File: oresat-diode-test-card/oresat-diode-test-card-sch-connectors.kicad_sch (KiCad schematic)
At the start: 13 parts, among them J1 J-SAMTEC-TFM-110-X1-XXX-D-RA, J2 U.FL, J3 U.FL, J4 U.FL, J6 J-SAMTEC-TFM-120-X1-XXX-D-RA

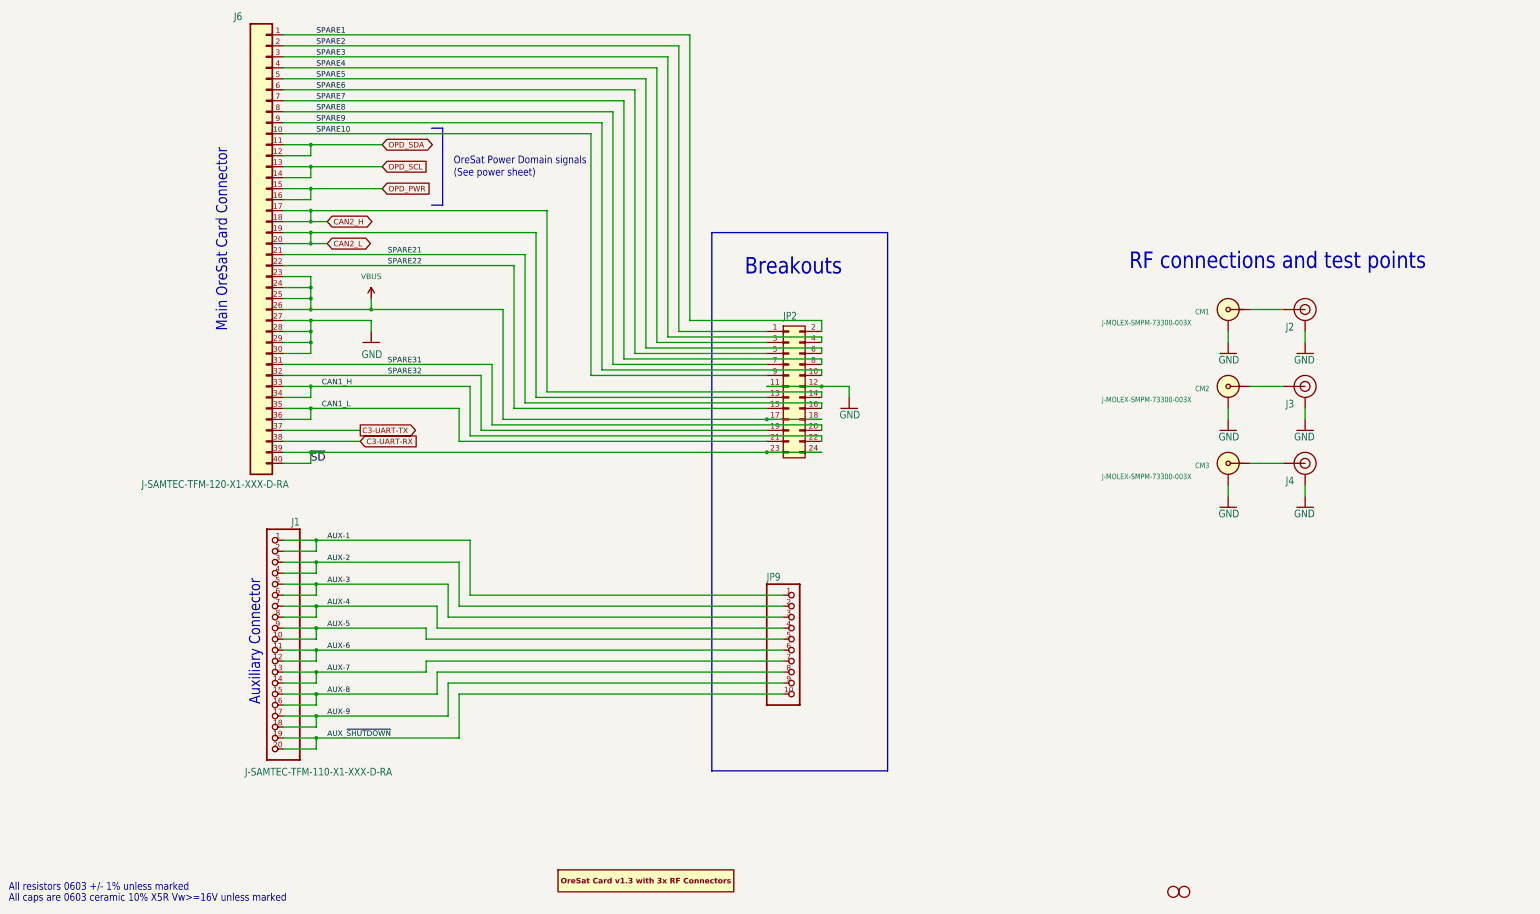
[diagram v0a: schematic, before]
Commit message: added photodiode and mux on schematic
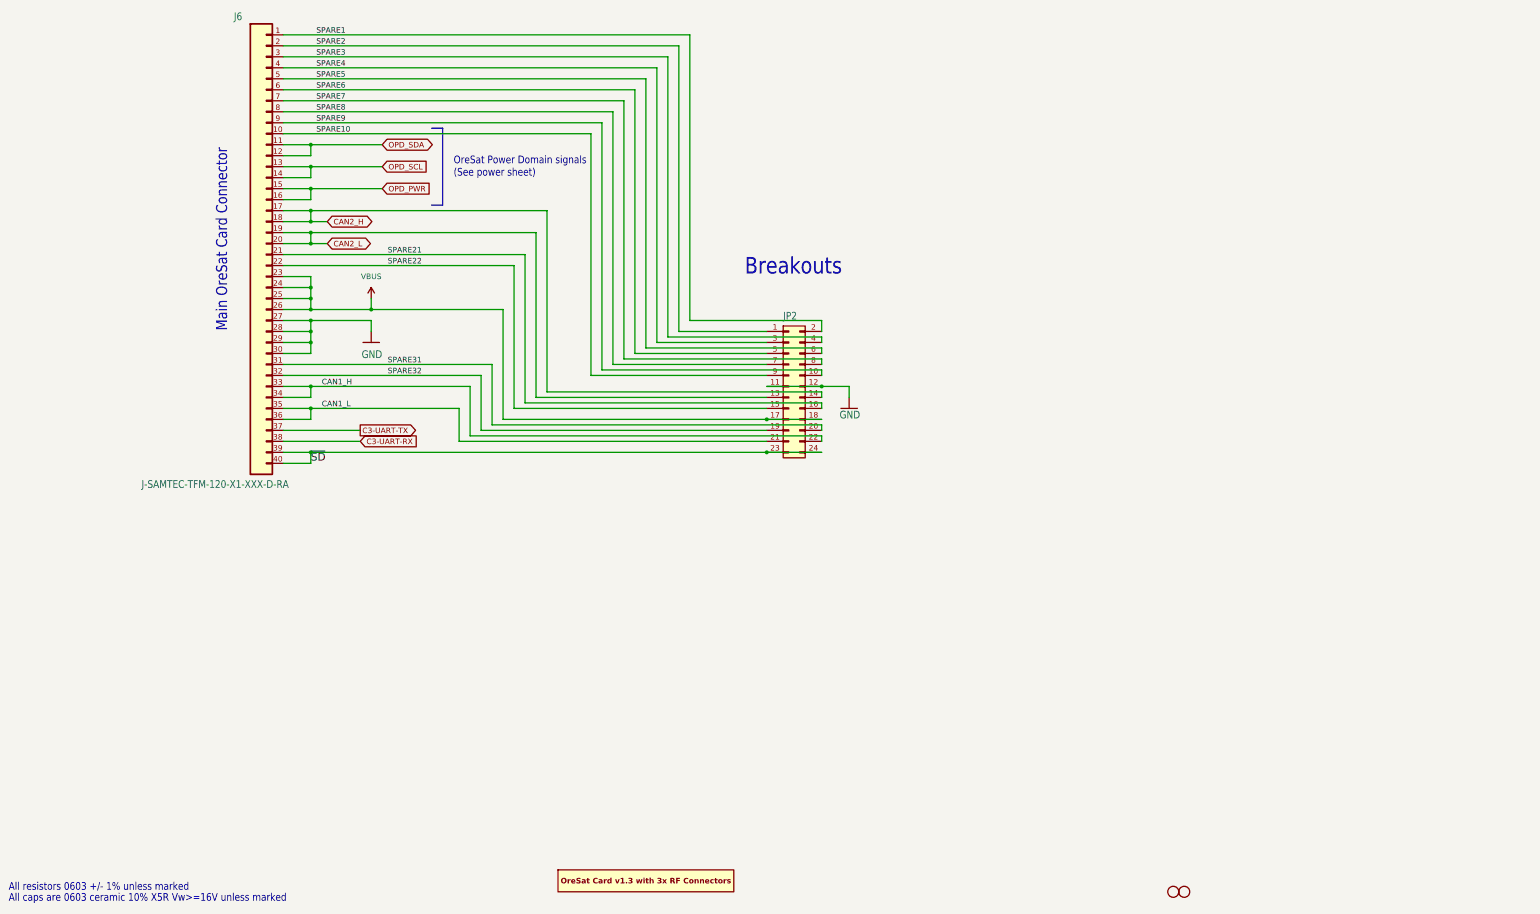
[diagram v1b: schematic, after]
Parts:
- removed CM1, CM2, CM3: J-MOLEX-SMPM-73300-003X, oresat-connectors:J-MOLEX-SMPM-073300-002X, symbol oresat-connectors:J-MOLEX-SMPM-73300-002X
- removed J1: J-SAMTEC-TFM-110-X1-XXX-D-RA, oresat-proto-card:J-SAMTEC-TFM-110-X1-XXX-D-RA, symbol oresat-proto-card-eagle-import:J-SAMTEC-TFM-110-X1-XXX-D-RA
- removed J2, J3, J4: U.FL, oresat-connectors:J-U.FL, symbol oresat-connectors:U.FL2PIN
- removed JP9: PINHD-1X10, oresat-proto-card:1X10, symbol oresat-proto-card-eagle-import:PINHD-1X10
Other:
- note removed: "Auxiliary Connector"
- note removed: "RF connections and test points"

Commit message: Quick design review on schematic; basically ready for layout.
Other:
- title: OreSat M0 Proto Card: Connectors -> OreSat Diode Test Card
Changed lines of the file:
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@@
 	(paper "USLedger")
 	(title_block
-		(title "OreSat M0 Proto Card: Connectors")
-		(date "2024-03-21")
-		(rev "5.0")
+		(title "OreSat Diode Test Card")
+		(date "2024-04-21")
+		(rev "v1.0")
 	)
 	(junction

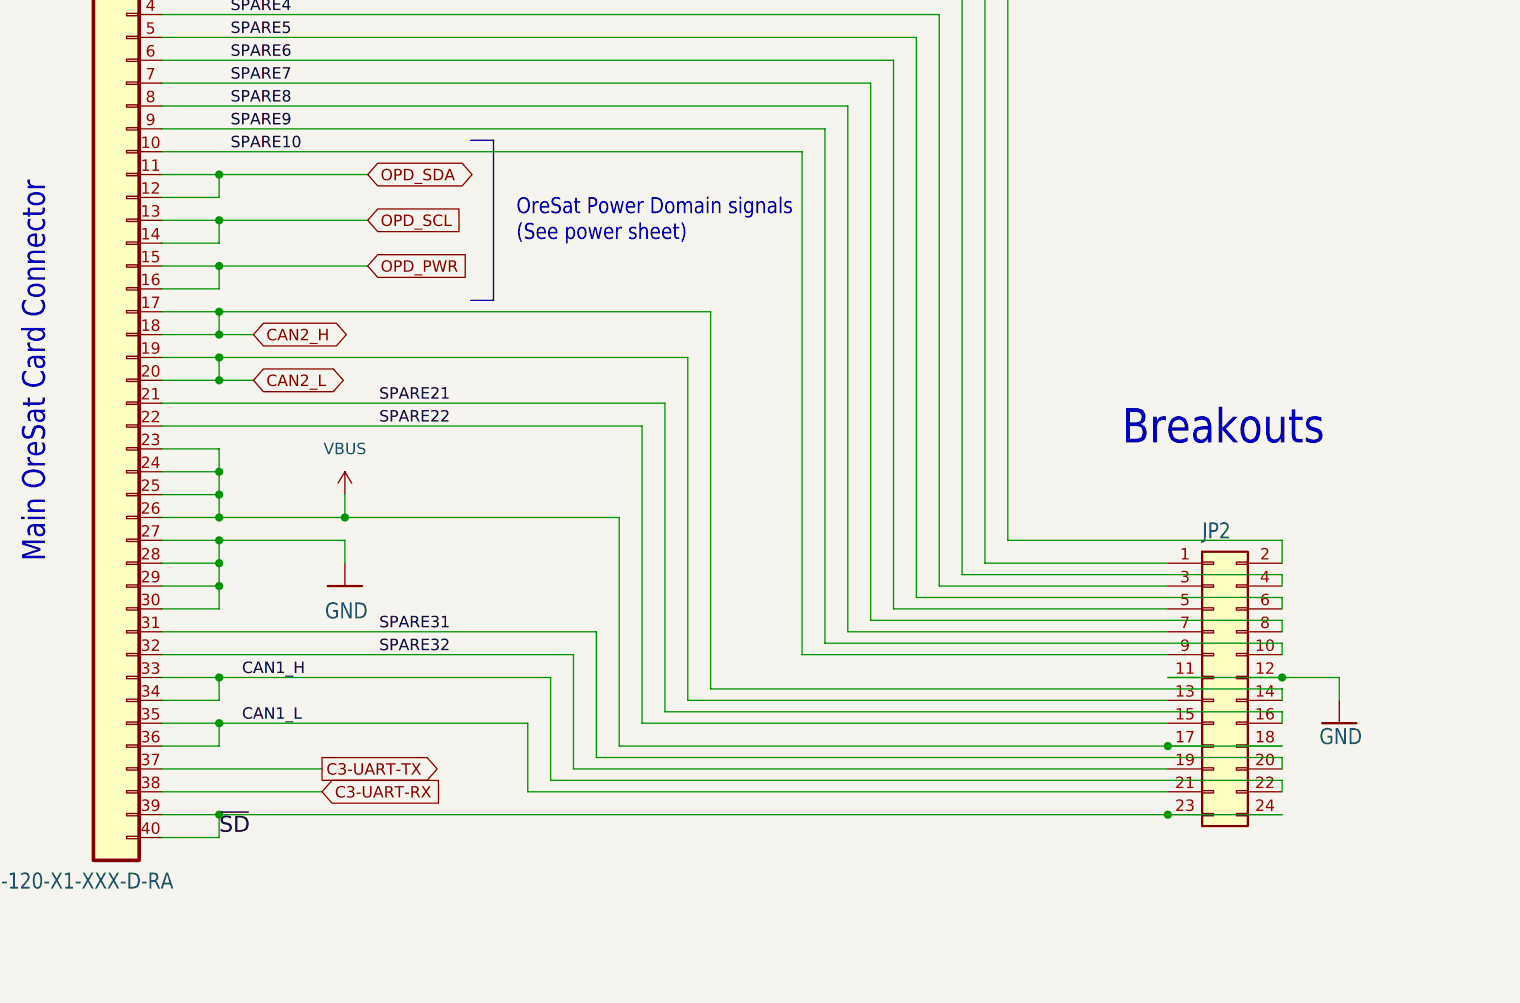
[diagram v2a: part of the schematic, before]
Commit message: Lots of schematic cleanup - replace weird ground and power symbols with more kicad ones, fix values, fix OPD connections and address, update PCB
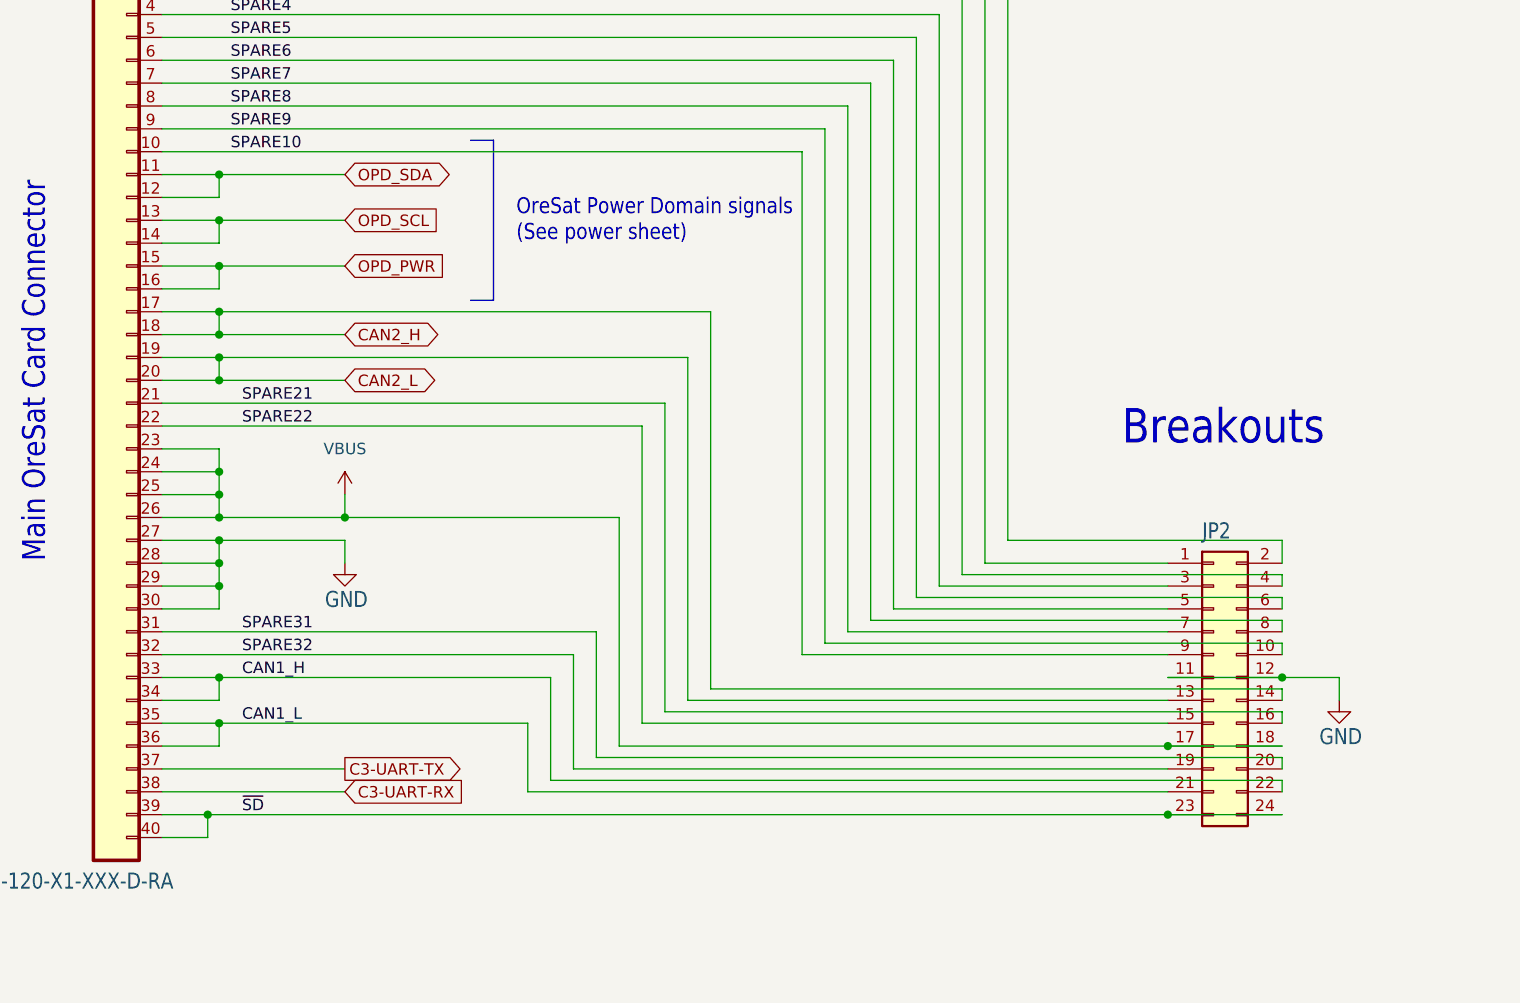
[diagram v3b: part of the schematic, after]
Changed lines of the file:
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@@
+	)
+	(junction
+		(at 83.82 144.78)
+		(diameter 0)
+		(color 0 0 0 0)
 	)
 	(junction
@@
 	)
 	(junction
-		(at 85.09 144.78)
-		(diameter 0)
-		(color 0 0 0 0)
-	)
-	(junction
 		(at 85.09 93.98)
 		(diameter 0)
@@
 	(wire
 		(pts
-			(xy 85.09 144.78) (xy 78.74 144.78)
-		)
-		(stroke
-			(width 0.1524)
-			(type solid)
-		)
-	)
-	(wire
-		(pts
 			(xy 78.74 129.54) (xy 85.09 129.54)
 		)
@@
 	(wire
 		(pts
+			(xy 83.82 147.32) (xy 78.74 147.32)
+		)
+		(stroke
+			(width 0.1524)
+			(type solid)
+		)
+	)
+	(wire
+		(pts
 			(xy 78.74 116.84) (xy 85.09 116.84)
 		)
@@
 	(wire
 		(pts
-			(xy 78.74 142.24) (xy 96.52 142.24)
+			(xy 78.74 142.24) (xy 99.06 142.24)
 		)
 		(stroke
@@
 	(wire
 		(pts
-			(xy 85.09 144.78) (xy 190.5 144.78)
-		)
-		(stroke
-			(width 0.1524)
-			(type solid)
-		)
-	)
-	(wire
-		(pts
-			(xy 78.74 147.32) (xy 85.09 147.32)
+			(xy 83.82 144.78) (xy 190.5 144.78)
 		)
 		(stroke
@@
 	(wire
 		(pts
-			(xy 101.6 78.74) (xy 85.09 78.74)
+			(xy 99.06 78.74) (xy 85.09 78.74)
 		)
 		(stroke
@@
 	(wire
 		(pts
+			(xy 83.82 144.78) (xy 78.74 144.78)
+		)
+		(stroke
+			(width 0.1524)
+			(type solid)
+		)
+	)
+	(wire
+		(pts
 			(xy 78.74 109.22) (xy 85.09 109.22)
 		)
@@
 	(wire
 		(pts
-			(xy 101.6 83.82) (xy 85.09 83.82)
+			(xy 99.06 83.82) (xy 85.09 83.82)
 		)
 		(stroke
@@
 	(wire
 		(pts
-			(xy 85.09 73.66) (xy 101.6 73.66)
+			(xy 85.09 73.66) (xy 99.06 73.66)
 		)
 		(stroke
@@
 	(wire
 		(pts
-			(xy 85.09 147.32) (xy 85.09 144.78)
-		)
-		(stroke
-			(width 0.1524)
-			(type solid)
-		)
-	)
-	(wire
-		(pts
 			(xy 99.06 109.22) (xy 99.06 111.76)
 		)
@@
 	(wire
 		(pts
-			(xy 78.74 139.7) (xy 96.52 139.7)
+			(xy 78.74 139.7) (xy 99.06 139.7)
 		)
 		(stroke
@@
 	(wire
 		(pts
-			(xy 85.09 91.44) (xy 88.9 91.44)
+			(xy 85.09 91.44) (xy 99.06 91.44)
 		)
 		(stroke
@@
 	(wire
 		(pts
+			(xy 83.82 144.78) (xy 83.82 147.32)
+		)
+		(stroke
+			(width 0.1524)
+			(type solid)
+		)
+	)
+	(wire
+		(pts
 			(xy 85.09 83.82) (xy 78.74 83.82)
 		)
@@
 	(wire
 		(pts
-			(xy 85.09 96.52) (xy 88.9 96.52)
+			(xy 85.09 96.52) (xy 99.06 96.52)
 		)
 		(stroke
@@
 	)
 	(label "SPARE22"
-		(at 102.87 101.6 0)
+		(at 87.63 101.6 0)
 		(fields_autoplaced yes)
 		(effects
@@
 	)
 	(label "SPARE21"
-		(at 102.87 99.06 0)
+		(at 87.63 99.06 0)
 		(fields_autoplaced yes)
 		(effects
@@
 	)
 	(label "~{SD}"
-		(at 85.09 147.32 0)
-		(fields_autoplaced yes)
-		(effects
-			(font
-				(size 1.778 1.778)
+		(at 87.63 144.78 0)
+		(fields_autoplaced yes)
+		(effects
+			(font
+				(size 1.27 1.27)
 			)
 			(justify left bottom)
@@
 	)
 	(label "SPARE32"
-		(at 102.87 127 0)
+		(at 87.63 127 0)
 		(fields_autoplaced yes)
 		(effects
@@
 	)
 	(label "SPARE31"
-		(at 102.87 124.46 0)
+		(at 87.63 124.46 0)
 		(fields_autoplaced yes)
 		(effects
@@
 	(global_label "OPD_PWR"
 		(shape input)
-		(at 101.6 83.82 0)
+		(at 99.06 83.82 0)
 		(fields_autoplaced yes)
 		(effects
@@
 		)
 		(property "Intersheetrefs" "${INTERSHEET_REFS}"
-			(at 113.4147 83.82 0)
+			(at 110.8747 83.82 0)
 			(effects
 				(font
@@
 	(global_label "C3-UART-RX"
 		(shape input)
-		(at 96.52 142.24 0)
+		(at 99.06 142.24 0)
 		(fields_autoplaced yes)
 		(effects
@@
 		)
 		(property "Intersheetrefs" "${INTERSHEET_REFS}"
-			(at 111.6936 142.1606 0)
+			(at 114.2336 142.1606 0)
 			(effects
 				(font
@@
 	(global_label "OPD_SDA"
 		(shape bidirectional)
-		(at 101.6 73.66 0)
+		(at 99.06 73.66 0)
 		(fields_autoplaced yes)
 		(effects
@@
 		)
 		(property "Intersheetrefs" "${INTERSHEET_REFS}"
-			(at 114.1027 73.66 0)
+			(at 111.5627 73.66 0)
 			(effects
 				(font
@@
 	(global_label "CAN2_L"
 		(shape bidirectional)
-		(at 88.9 96.52 0)
+		(at 99.06 96.52 0)
 		(fields_autoplaced yes)
 		(effects
@@
 		)
 		(property "Intersheetrefs" "${INTERSHEET_REFS}"
-			(at 99.8908 96.52 0)
+			(at 110.0508 96.52 0)
 			(effects
 				(font
@@
 	(global_label "C3-UART-TX"
 		(shape output)
-		(at 96.52 139.7 0)
+		(at 99.06 139.7 0)
 		(fields_autoplaced yes)
 		(effects
@@
 		)
 		(property "Intersheetrefs" "${INTERSHEET_REFS}"
-			(at 111.8839 139.7 0)
+			(at 114.4239 139.7 0)
 			(effects
 				(font
@@
 	(global_label "CAN2_H"
 		(shape bidirectional)
-		(at 88.9 91.44 0)
+		(at 99.06 91.44 0)
 		(fields_autoplaced yes)
 		(effects
@@
 		)
 		(property "Intersheetrefs" "${INTERSHEET_REFS}"
-			(at 100.1932 91.44 0)
+			(at 110.3532 91.44 0)
 			(effects
 				(font
@@
 	(global_label "OPD_SCL"
 		(shape input)
-		(at 101.6 78.74 0)
+		(at 99.06 78.74 0)
 		(fields_autoplaced yes)
 		(effects
@@
 		)
 		(property "Intersheetrefs" "${INTERSHEET_REFS}"
-			(at 112.9309 78.74 0)
+			(at 110.3909 78.74 0)
 			(effects
 				(font
@@
 	)
 	(symbol
-		(lib_id "oresat-proto-card-eagle-import:GND")
-		(at 209.55 134.62 0)
+		(lib_id "power:GND")
+		(at 209.55 132.08 0)
 		(mirror y)
 		(unit 1)
@@
 		(dnp no)
 		(property "Reference" "#GND038"
-			(at 209.55 134.62 0)
+			(at 209.55 132.08 0)
 			(effects
 				(font
@@
 		)
 		(property "Footprint" ""
-			(at 209.55 134.62 0)
+			(at 209.55 132.08 0)
 			(effects
 				(font
@@
 		)
 		(property "Datasheet" ""
-			(at 209.55 134.62 0)
-			(effects
-				(font
-					(size 1.27 1.27)
-				)
-				(hide yes)
-			)
-		)
-		(property "Description" ""
-			(at 209.55 134.62 0)
+			(at 209.55 132.08 0)
+			(effects
+				(font
+					(size 1.27 1.27)
+				)
+				(hide yes)
+			)
+		)
+		(property "Description" "Power symbol creates a global label with name \"GND\" , ground"
+			(at 209.55 132.08 0)
 			(effects
 				(font
@@
 	)
 	(symbol
-		(lib_id "oresat-proto-card-eagle-import:GND")
-		(at 99.06 119.38 0)
+		(lib_id "power:GND")
+		(at 99.06 116.84 0)
 		(mirror y)
 		(unit 1)
@@
 		(dnp no)
 		(property "Reference" "#GND02"
-			(at 99.06 119.38 0)
+			(at 99.06 116.84 0)
 			(effects
 				(font
@@
 		)
 		(property "Value" "GND"
-			(at 101.6 123.19 0)
+			(at 101.6 121.92 0)
 			(effects
 				(font
@@
 		)
 		(property "Footprint" ""
-			(at 99.06 119.38 0)
+			(at 99.06 116.84 0)
 			(effects
 				(font
@@
 		)
 		(property "Datasheet" ""
-			(at 99.06 119.38 0)
-			(effects
-				(font
-					(size 1.27 1.27)
-				)
-				(hide yes)
-			)
-		)
-		(property "Description" ""
-			(at 99.06 119.38 0)
-			(effects
-				(font
+			(at 99.06 116.84 0)
+			(effects
+				(font
+					(size 1.27 1.27)
+				)
+				(hide yes)
+			)
+		)
+		(property "Description" "Power symbol creates a global label with name \"GND\" , ground"
+			(at 99.06 116.84 0)
+			(effects
+				(font

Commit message: updated layout and schematic with correct values
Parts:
- PCB1: value ORESAT-CARD-V1.3-3RF -> ORESAT-CARD-V1.0-0xRF; footprint oresat-pcbs:ORESAT-CARD-V1.3-3RF -> oresat-pcbs:ORESAT-CARD-V1.3-0RF
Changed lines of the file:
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@@
 			)
 		)
-		(property "Value" "ORESAT-CARD-V1.3-3RF"
+		(property "Value" "ORESAT-CARD-V1.0-0xRF"
 			(at 162.56 238.76 0)
 			(effects
@@
 			)
 		)
-		(property "Footprint" "oresat-pcbs:ORESAT-CARD-V1.3-3RF"
+		(property "Footprint" "oresat-pcbs:ORESAT-CARD-V1.3-0RF"
 			(at 162.56 232.41 0)
 			(effects
